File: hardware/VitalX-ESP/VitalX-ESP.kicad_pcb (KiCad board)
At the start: 4 copper layers, 73 x 63 mm, 56 parts, among them J1 ECG Probe, J2 GSR Probe, J3 UART, J4 JTAG, J5 Power terminal, Q1 BSS138, SW2 Reset, U1 AD8232ACPZ-R7, U3 ADP160AUJZ-1.8-R7, U4 ADPD144RI-ACEZ-RL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

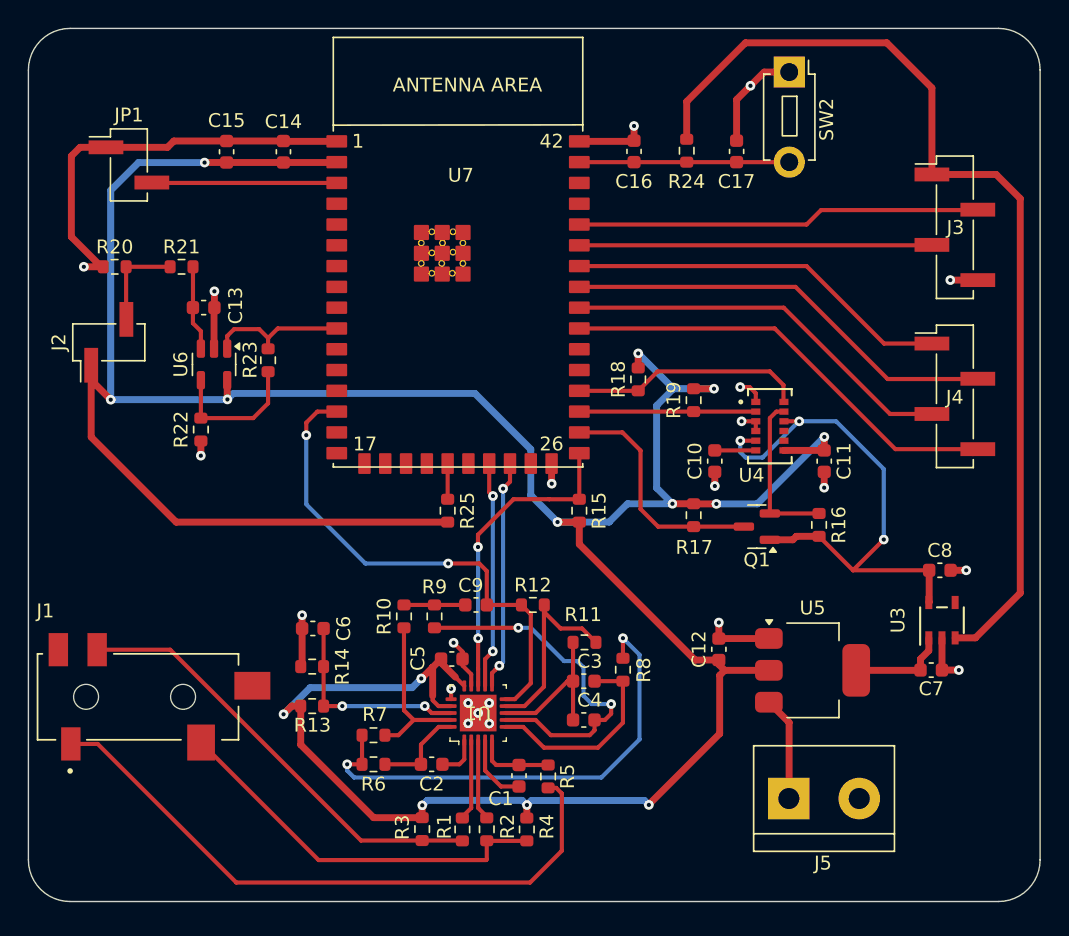
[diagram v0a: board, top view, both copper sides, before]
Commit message: [nightly] Switch to through via only.
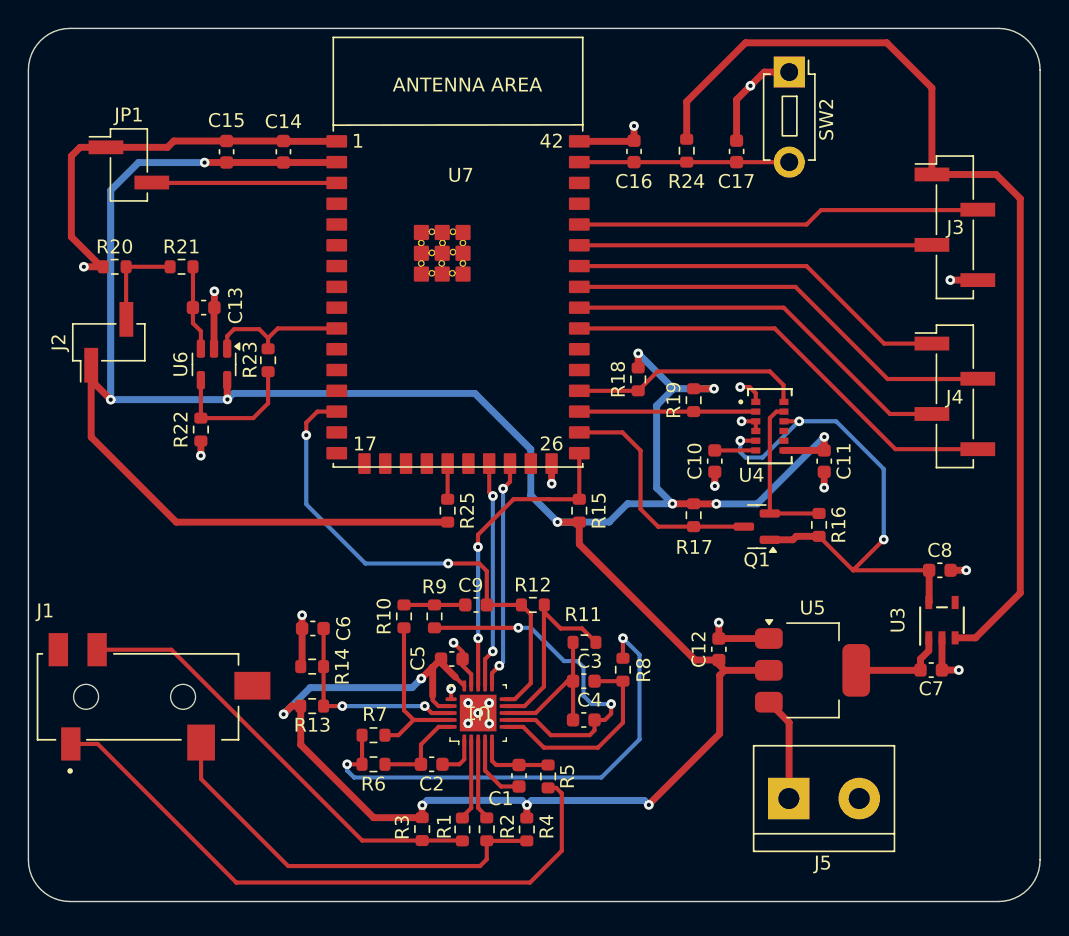
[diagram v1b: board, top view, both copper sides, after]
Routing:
- net RA: track 28.4 -> 30.3 mm
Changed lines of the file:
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@@
   (segment (start 153.46 75.35) (end 153.45 75.35) (width 0.3) (layer "F.Cu") (net 8))
   (segment (start 151.82 91.025) (end 151.82 89.87) (width 0.5) (layer "F.Cu") (net 8))
-  (via micro (at 169.14 93.3) (size 0.7) (drill 0.3) (layers "F.Cu" "In1.Cu") (net 8))
-  (via micro (at 169.67 86.1) (size 0.7) (drill 0.3) (layers "F.Cu" "In1.Cu") (net 8))
-  (via micro (at 153.46 75.35) (size 0.7) (drill 0.3) (layers "F.Cu" "In1.Cu") (net 8))
-  (via micro (at 159.42 80.14) (size 0.7) (drill 0.3) (layers "F.Cu" "In1.Cu") (net 8))
-  (via micro (at 145.7 54.04) (size 0.7) (drill 0.3) (layers "F.Cu" "In1.Cu") (net 8))
-  (via micro (at 168.52 65.16) (size 0.7) (drill 0.3) (layers "F.Cu" "In1.Cu") (net 8))
-  (via micro (at 121.75 89.34) (size 0.7) (drill 0.3) (layers "F.Cu" "In1.Cu") (net 8))
-  (via micro (at 132.68 91.33) (size 0.7) (drill 0.3) (layers "F.Cu" "In1.Cu") (net 8))
-  (via micro (at 151.82 89.87) (size 0.7) (drill 0.3) (layers "F.Cu" "In1.Cu") (net 8))
-  (via micro (at 135.25 95.68) (size 0.7) (drill 0.3) (layers "F.Cu" "In1.Cu") (net 8))
-  (via micro (at 114.44 77.83) (size 0.7) (drill 0.3) (layers "F.Cu" "In1.Cu") (net 8))
-  (via micro (at 115.42 65.97) (size 0.7) (drill 0.3) (layers "F.Cu" "In1.Cu") (net 8))
-  (via micro (at 134.452399 96.399999) (size 0.7) (drill 0.3) (layers "F.Cu" "In1.Cu") (net 8))
-  (via micro (at 151.53 80.02) (size 0.7) (drill 0.3) (layers "F.Cu" "In1.Cu") (net 8))
-  (via micro (at 133.73 97.15) (size 0.7) (drill 0.3) (layers "F.Cu" "In1.Cu") (net 8))
-  (via micro (at 153.36 72.88) (size 0.7) (drill 0.3) (layers "F.Cu" "In1.Cu") (net 8))
-  (via micro (at 154.1 51.14) (size 0.7) (drill 0.3) (layers "F.Cu" "In1.Cu") (net 8))
-  (via micro (at 135.26 97.16) (size 0.7) (drill 0.3) (layers "F.Cu" "In1.Cu") (net 8))
-  (via micro (at 133.73 95.68) (size 0.7) (drill 0.3) (layers "F.Cu" "In1.Cu") (net 8))
-  (via micro (at 106 64.2) (size 0.7) (drill 0.3) (layers "F.Cu" "In1.Cu") (net 8))
-  (via micro (at 132.5 94.65) (size 0.7) (drill 0.3) (layers "F.Cu" "In1.Cu") (net 8))
-  (via micro (at 139.76 79.85) (size 0.7) (drill 0.3) (layers "F.Cu" "In1.Cu") (net 8))
+  (via (at 169.14 93.3) (size 0.7) (drill 0.3) (layers "F.Cu" "B.Cu") (net 8))
+  (via (at 169.67 86.1) (size 0.7) (drill 0.3) (layers "F.Cu" "B.Cu") (net 8))
+  (via (at 153.46 75.35) (size 0.7) (drill 0.3) (layers "F.Cu" "B.Cu") (net 8))
+  (via (at 159.42 80.14) (size 0.7) (drill 0.3) (layers "F.Cu" "B.Cu") (net 8))
+  (via (at 145.7 54.04) (size 0.7) (drill 0.3) (layers "F.Cu" "B.Cu") (net 8))
+  (via (at 168.52 65.16) (size 0.7) (drill 0.3) (layers "F.Cu" "B.Cu") (net 8))
+  (via (at 121.75 89.34) (size 0.7) (drill 0.3) (layers "F.Cu" "B.Cu") (net 8))
+  (via (at 132.68 91.33) (size 0.7) (drill 0.3) (layers "F.Cu" "B.Cu") (net 8))
+  (via (at 151.82 89.87) (size 0.7) (drill 0.3) (layers "F.Cu" "B.Cu") (net 8))
+  (via (at 135.25 95.68) (size 0.7) (drill 0.3) (layers "F.Cu" "B.Cu") (net 8))
+  (via (at 114.44 77.83) (size 0.7) (drill 0.3) (layers "F.Cu" "B.Cu") (net 8))
+  (via (at 115.42 65.97) (size 0.7) (drill 0.3) (layers "F.Cu" "B.Cu") (net 8))
+  (via (at 134.452399 96.399999) (size 0.7) (drill 0.3) (layers "F.Cu" "B.Cu") (net 8))
+  (via (at 151.53 80.02) (size 0.7) (drill 0.3) (layers "F.Cu" "B.Cu") (net 8))
+  (via (at 133.73 97.15) (size 0.7) (drill 0.3) (layers "F.Cu" "B.Cu") (net 8))
+  (via (at 153.36 72.88) (size 0.7) (drill 0.3) (layers "F.Cu" "B.Cu") (net 8))
+  (via (at 154.1 51.14) (size 0.7) (drill 0.3) (layers "F.Cu" "B.Cu") (net 8))
+  (via (at 135.26 97.16) (size 0.7) (drill 0.3) (layers "F.Cu" "B.Cu") (net 8))
+  (via (at 133.73 95.68) (size 0.7) (drill 0.3) (layers "F.Cu" "B.Cu") (net 8))
+  (via (at 106 64.2) (size 0.7) (drill 0.3) (layers "F.Cu" "B.Cu") (net 8))
+  (via (at 132.5 94.65) (size 0.7) (drill 0.3) (layers "F.Cu" "B.Cu") (net 8))
+  (via (at 139.76 79.85) (size 0.7) (drill 0.3) (layers "F.Cu" "B.Cu") (net 8))
   (segment (start 123.3 93.05) (end 123.3 90.3) (width 0.3) (layer "F.Cu") (net 9))
   (segment (start 123.3 95.9) (end 123.3 93.05) (width 0.3) (layer "F.Cu") (net 9))
@@
   (segment (start 145.7 56.65) (end 141.75 56.65) (width 0.3) (layer "F.Cu") (net 16))
   (segment (start 153.1 56.65) (end 149.5 56.65) (width 0.3) (layer "F.Cu") (net 16))
-  (segment (start 135.02 107.01) (end 135.0725 106.9575) (width 0.3) (layer "F.Cu") (net 17))
+  (segment (start 120.741 107.442) (end 134.588 107.442) (width 0.3) (layer "F.Cu") (net 17))
   (segment (start 137.9625 105.625) (end 135.0825 105.625) (width 0.3) (layer "F.Cu") (net 17))
   (segment (start 135.17 105.625) (end 135.16 105.615) (width 0.3) (layer "F.Cu") (net 17))
-  (segment (start 114.46 98.53) (end 122.94 107.01) (width 0.3) (layer "F.Cu") (net 17))
   (segment (start 135.0725 106.9575) (end 135.0725 105.615) (width 0.3) (layer "F.Cu") (net 17))
-  (segment (start 122.94 107.01) (end 135.02 107.01) (width 0.3) (layer "F.Cu") (net 17))
+  (segment (start 114.46 101.161) (end 120.741 107.442) (width 0.3) (layer "F.Cu") (net 17))
+  (segment (start 114.46 98.53) (end 114.46 101.161) (width 0.3) (layer "F.Cu") (net 17))
+  (segment (start 134.588 107.442) (end 135.0725 106.9575) (width 0.3) (layer "F.Cu") (net 17))
   (segment (start 138.2 108.63) (end 117 108.63) (width 0.3) (layer "F.Cu") (net 18))
   (segment (start 107 98.63) (end 105.06 98.63) (width 0.3) (layer "F.Cu") (net 18))
@@
   (segment (start 144.86 76.15) (end 146.17 77.46) (width 0.3) (layer "F.Cu") (net 28))
   (segment (start 147.439999 82.949999) (end 150 82.949999) (width 0.3) (layer "F.Cu") (net 28))
-  (segment (start 106.96 91.83) (end 112.23 91.83) (width 0.3) (layer "F.Cu") (net 29))
-  (segment (start 126 105.6) (end 130.4125 105.6) (width 0.3) (layer "F.Cu") (net 29))
-  (segment (start 112.23 91.83) (end 126 105.6) (width 0.3) (layer "F.Cu") (net 29))
+  (segment (start 112.317 91.83) (end 126.087 105.6) (width 0.3) (layer "F.Cu") (net 29))
   (segment (start 130.4125 105.6) (end 133.2875 105.6) (width 0.3) (layer "F.Cu") (net 29))
+  (segment (start 126.087 105.6) (end 130.4125 105.6) (width 0.3) (layer "F.Cu") (net 29))
+  (segment (start 106.96 91.83) (end 112.317 91.83) (width 0.3) (layer "F.Cu") (net 29))
   (segment (start 133.9524 98.352398) (end 133.9524 103.2476) (width 0.3) (layer "F.Cu") (net 30))
   (segment (start 133.3125 103.8875) (end 133.9524 103.2476) (width 0.3) (layer "F.Cu") (net 30))
@@
     (connect_pads yes (clearance 0.5))
     (min_thickness 0.25) (filled_areas_thickness no)
-    (fill yes (thermal_gap 0.5) (thermal_bridge_width 0.5))
+    (fill (thermal_gap 0.5) (thermal_bridge_width 0.5))
     (polygon
       (pts

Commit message: [nighly] Various PCB update.
PCB stack-up change: Signal-GND-Power(3.3V)-Signal
Track width in mil: 10, 15, 20, 42
Via size in mil(dia/hole): 20/10, 15/30
Show ECG Probe 3D model
Obfuscate 1.8V track
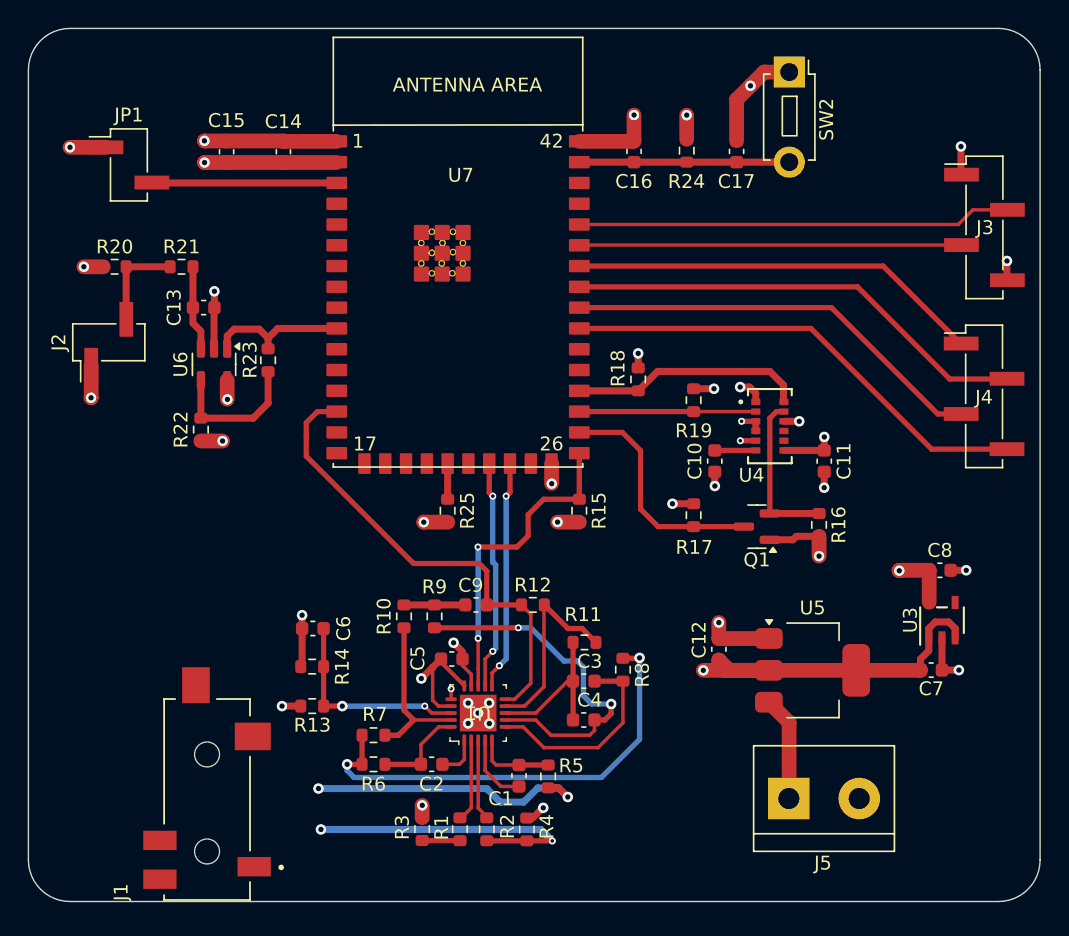
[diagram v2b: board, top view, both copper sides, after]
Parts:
- J1: value ECG Probe -> ECG Probe connector
- J2: value GSR Probe -> GSR Probe connector
- moved J1 8.93 mm to (114.9, 102.6), turned to 90 degrees
- moved J3 2.14 mm to (171.0, 61.4)
- moved J4 2.11 mm to (171.0, 73.5)
- moved R1 0.17 mm to (133.1, 104.8), turned to -90 degrees
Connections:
- J1 pad S: RL -> RA
- J1 pad T: RA -> RL
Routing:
- net +3V3: track 317.3 -> 67.7 mm, vias 14 -> 16
- net LA: track 32.0 -> 2.75 mm
- net RL: track 45.8 -> 20.8 mm, vias 0 -> 2
- net GND: track 74.7 -> 59.1 mm, vias 22 -> 24
- net RA: track 30.3 -> 21.8 mm, vias 0 -> 2
- net +1V8: track 39.2 -> 33.6 mm, vias 3 -> 4
- net Net-(R6-Pad2): track 35.3 -> 33.2 mm
- net Net-(J3-Pin_3): track 25.5 -> 27.6 mm
- net Net-(J3-Pin_2): track 29.2 -> 31.3 mm
- net /TMS: track 27.8 -> 29.9 mm
- net /TDI: track 31.5 -> 33.6 mm
- net /TDO: track 28.6 -> 30.7 mm
- net ECG_OUT: track 36.6 -> 34.6 mm, vias 2 -> 0
- net /TCK: track 32.9 -> 34.5 mm
- added copper zone on In2.Cu, net +3V3
- removed copper zone on In2.Cu, net GND
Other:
- board text removed: "Considering USB connector."

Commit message: [nightly] Program/Debug interface.
Implementing proper program connector (2x3) and jtag (2x5)
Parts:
- J3: value UART -> PROG; footprint Connector_PinHeader_2.54mm:PinHeader_1x04_P2.54mm_Vertical_SMD_Pin1Left -> Connector_PinHeader_2.54mm:PinHeader_2x03_P2.54mm_Vertical
- J4: footprint Connector_PinHeader_2.54mm:PinHeader_1x04_P2.54mm_Vertical_SMD_Pin1Left -> Connector_PinHeader_2.54mm:PinHeader_2x05_P2.54mm_Vertical
- moved J4 5.81 mm to (173.2, 78.9), turned to 180 degrees
- moved J3 4.77 mm to (170.7, 56.6)
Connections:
- net Net-(J3-Pin_3) renamed /TXD
- J3 pad 1: +3V3 -> /ESP32_EN
- J3 pad 2: Net-(J3-Pin_2) -> +3V3
- J4 pad 1: /TMS -> +3V3
- J4 pad 2: /TDI -> /TMS
- J4 pad 3: /TDO -> GND
- U7 pad 38: Net-(J3-Pin_2) -> /RXD
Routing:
- net /GPIO0: track 13.4 -> 70.7 mm, vias 0 -> 1
- net /RXD: track 0.00 -> 33.9 mm, vias 0 -> 1
- net Net-(J3-Pin_2): track 31.3 -> 0.00 mm
- net LA: track 2.75 -> 24.3 mm
- net /ESP32_EN: track 15.2 -> 29.0 mm
- net /TMS: track 29.9 -> 40.7 mm, vias 0 -> 1
- net RL: track 20.8 -> 28.1 mm
- net RA: track 21.8 -> 28.1 mm
- net /TXD: track 27.6 -> 30.4 mm
- net /TDI: track 33.6 -> 31.2 mm
- net /TCK: track 34.5 -> 32.1 mm
- net +3V3: track 67.7 -> 69.8 mm
- net GND: track 59.1 -> 57.7 mm, vias 24 -> 35
- net /TDO: track 30.7 -> 31.7 mm

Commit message: [nightly] Various footprint update.
Change footprints:
- Reset button
- GSR conn header
Minor PCB changes:
- Increase thermal relief via size
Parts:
- added R26: 0, Resistor_SMD:R_0603_1608Metric, F.Cu at (144.9, 89.8)
- J2: footprint Connector_PinHeader_2.54mm:PinHeader_1x02_P2.54mm_Vertical_SMD_Pin1Left -> Connector_PinHeader_2.54mm:PinHeader_1x02_P2.54mm_Vertical
- SW2: footprint Button_Switch_THT:SW_PUSH_1P1T_6x3.5mm_H5.0_APEM_MJTP1250 -> Button_Switch_SMD:SW_Tactile_SPST_NO_Straight_CK_PTS636Sx25SMTRLFS
- moved J5 3.61 mm to (155.4, 105.9)
- moved SW2 2.64 mm to (156.8, 52.8)
- moved J2 1.73 mm to (109.0, 70.8), turned to 180 degrees
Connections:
- R6 pad 2: Net-(R6-Pad2) -> Net-(R26-Pad2)
- R7 pad 2: Net-(R6-Pad2) -> Net-(R26-Pad2)
- R8 pad 1: Net-(R6-Pad2) -> Net-(R26-Pad1)
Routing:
- net Net-(R26-Pad2): track 0.00 -> 37.3 mm, vias 0 -> 2
- net Net-(R6-Pad2): track 33.2 -> 0.00 mm, vias 2 -> 0
- net +5V: track 7.56 -> 10.3 mm
- net +3V3: track 69.8 -> 67.5 mm, vias 16 -> 15
- net Net-(R26-Pad1): track 0.00 -> 1.82 mm
- net GND: track 57.7 -> 59.1 mm

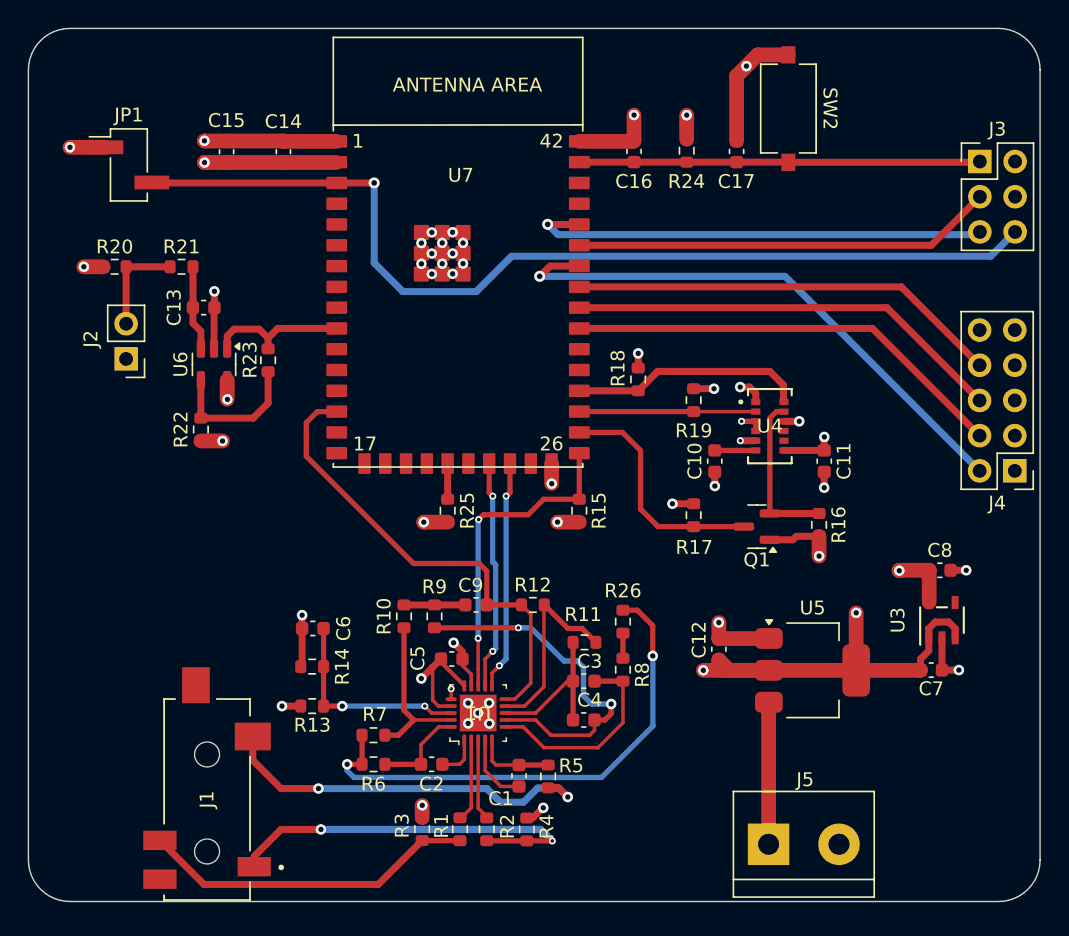
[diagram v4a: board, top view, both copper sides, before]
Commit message: [nightly] Various footprint update.
Footprint changes:
- Boot select SMD -> Through-hole
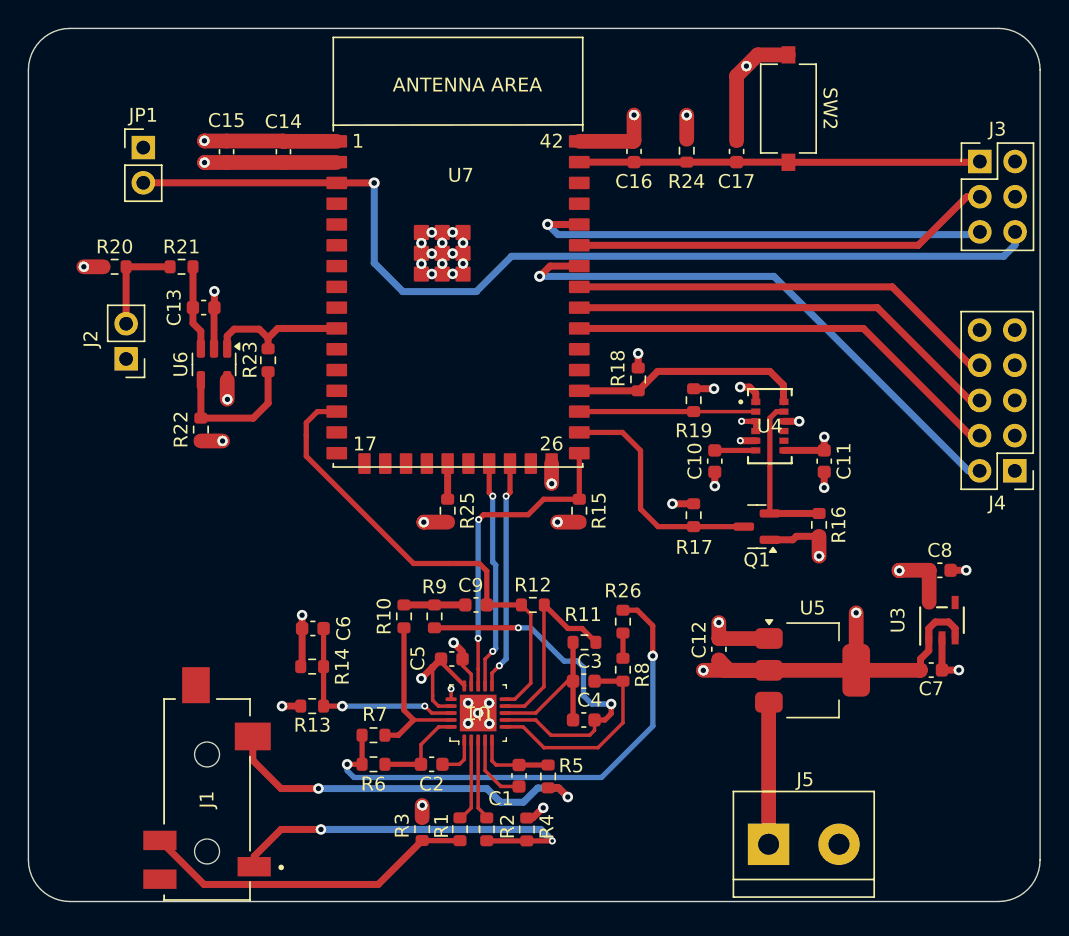
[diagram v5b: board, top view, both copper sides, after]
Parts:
- JP1: footprint Connector_PinHeader_2.54mm:PinHeader_1x02_P2.54mm_Vertical_SMD_Pin1Left -> Connector_PinHeader_2.54mm:PinHeader_1x02_P2.54mm_Vertical
- moved JP1 1.63 mm to (110.3, 55.6)
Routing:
- net GND: track 59.1 -> 56.5 mm, vias 35 -> 34
- net /GPIO0: track 70.7 -> 71.9 mm
